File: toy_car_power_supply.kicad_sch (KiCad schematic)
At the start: 17 parts, among them J1 Barrel_Jack_Switch, J2 Screw_Terminal_01x02, J3 Screw_Terminal_01x02, J4 Conn_01x03_Pin, J5 Conn_01x02_Pin, J6 Conn_01x03_Pin, J7 Conn_01x02_Pin, SW1 SW_Wuerth_450301014042, U1 LM317_TO-220, U2 LM7805_TO220

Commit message: Changes sheet name
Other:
- title: Kicad Power supply Board -> Power supply Board
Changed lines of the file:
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@@
   (paper "A4")
   (title_block
-    (title "Kicad Power supply Board")
+    (title "Power supply Board")
     (date "2024-07-30")
     (rev "1")

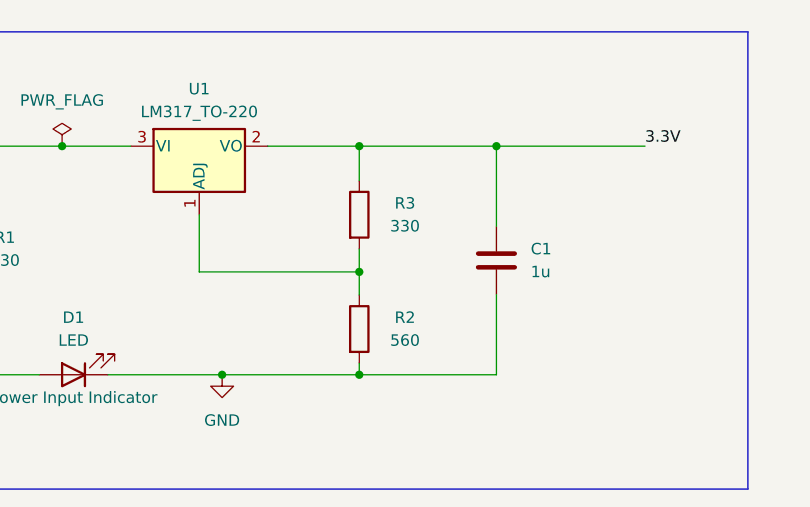
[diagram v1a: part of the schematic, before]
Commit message: Updated resistance value r1 = 270 r2 = 470
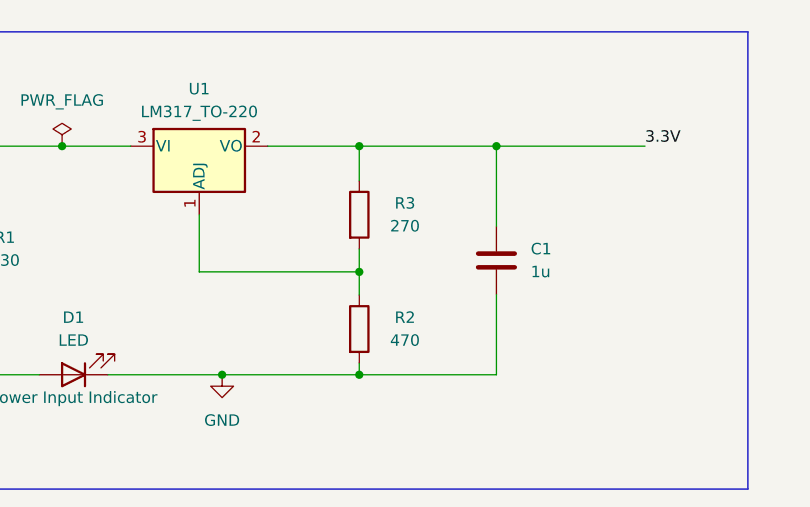
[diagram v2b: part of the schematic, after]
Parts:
- R2: value 560 -> 470
- R3: value 330 -> 270
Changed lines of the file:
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@@
       (effects (font (size 1.27 1.27)))
     )
-    (property "Value" "330" (at 91.44 114.3 0)
+    (property "Value" "270" (at 91.44 114.3 0)
       (effects (font (size 1.27 1.27)))
     )
@@
     (property "Datasheet" "~" (at 86.36 113.03 0)
       (effects (font (size 1.27 1.27)) hide)
+    )
+    (property "Purpose" "" (at 86.36 113.03 0)
+      (effects (font (size 1.27 1.27)))
     )
     (pin "1")
@@
       (effects (font (size 1.27 1.27)))
     )
-    (property "Value" "560" (at 91.44 127 0)
+    (property "Value" "470" (at 91.44 127 0)
       (effects (font (size 1.27 1.27)))
     )
@@
       (effects (font (size 1.27 1.27)) hide)
     )
+    (property "Purpose" "" (at 86.36 125.73 0)
+      (effects (font (size 1.27 1.27)))
+    )
     (pin "1")

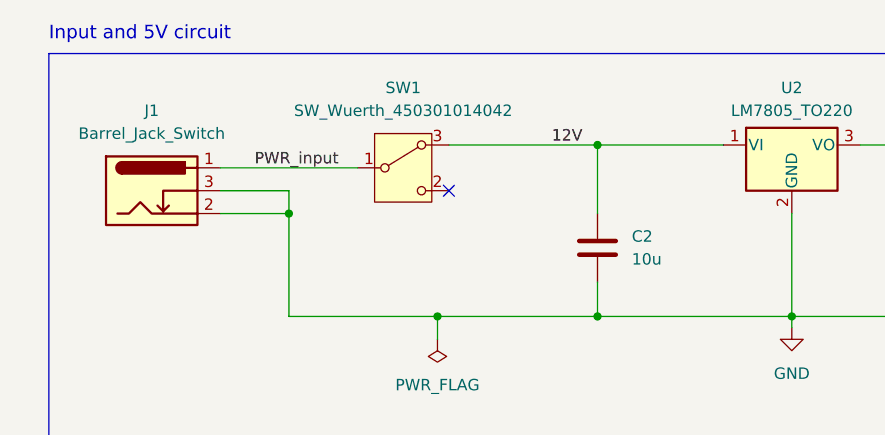
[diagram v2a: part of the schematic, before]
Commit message: Updated with custom switch with 4 pin
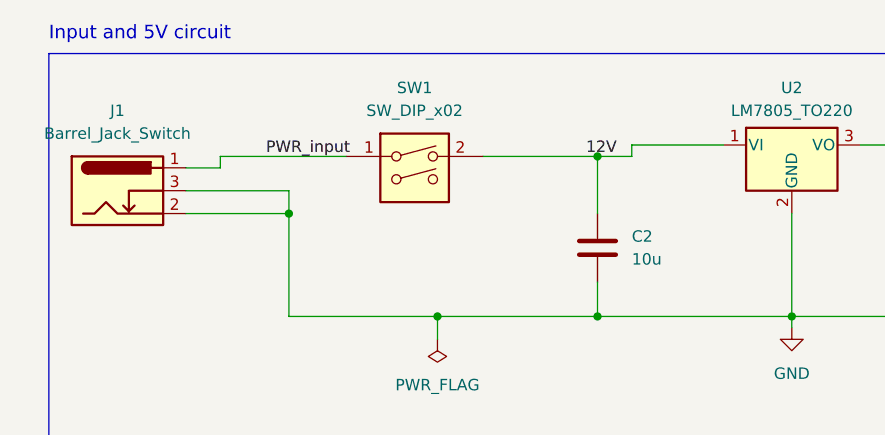
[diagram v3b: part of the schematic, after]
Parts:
- removed SW1: SW_Wuerth_450301014042, Button_Switch_THT:SW_Slide-03_Wuerth-WS-SLTV_10x2.5x6.4_P2.54mm, symbol Switch:SW_Wuerth_450301014042
- added SW1: SW_DIP_x02, custom_switch:DIP-4_W7.62mm, symbol custom_switch:SW_DIP_x02
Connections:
- net 12V: now also SW1.2
- net PWR_input: now also SW1.1
- no-connect marks 1 -> 0
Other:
- moved on the sheet: J1
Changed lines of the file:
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@@
     (company "Hobbyst")
   )
-  (junction (at 83.82 35.56) (diameter 0) (color 0 0 0 0)
-  )
   (junction (at 53.34 105.41) (diameter 0) (color 0 0 0 0)
   )
@@
   (junction (at 203.2 119.38) (diameter 0) (color 0 0 0 0)
   )
-  (no_connect (at 67.31 40.64))
+  (junction (at 83.82 36.83) (diameter 0) (color 0 0 0 0)
+  )
   (wire (pts (xy 223.52 90.17) (xy 214.63 90.17))
     (stroke (width 0) (type default))
   )
+  (wire (pts (xy 38.1 38.1) (xy 41.91 38.1))
+    (stroke (width 0) (type default))
+  )
   (wire (pts (xy 214.63 90.17) (xy 214.63 102.87))
     (stroke (width 0) (type default))
@@
     (stroke (width 0) (type default))
   )
+  (wire (pts (xy 41.91 36.83) (xy 55.88 36.83))
+    (stroke (width 0) (type default))
+  )
   (wire (pts (xy 41.91 120.65) (xy 41.91 130.81))
     (stroke (width 0) (type default))
@@
     (stroke (width 0) (type default))
   )
+  (wire (pts (xy 87.63 35.56) (xy 97.79 35.56))
+    (stroke (width 0) (type default))
+  )
   (wire (pts (xy 101.6 121.92) (xy 101.6 130.81))
     (stroke (width 0) (type default))
   )
-  (wire (pts (xy 41.91 40.64) (xy 49.53 40.64))
+  (wire (pts (xy 38.1 40.64) (xy 49.53 40.64))
     (stroke (width 0) (type default))
   )
@@
     (stroke (width 0) (type default))
   )
-  (wire (pts (xy 41.91 38.1) (xy 57.15 38.1))
-    (stroke (width 0) (type default))
-  )
   (wire (pts (xy 49.53 43.18) (xy 49.53 54.61))
     (stroke (width 0) (type default))
@@
     (stroke (width 0) (type default))
   )
+  (wire (pts (xy 83.82 36.83) (xy 87.63 36.83))
+    (stroke (width 0) (type default))
+  )
   (wire (pts (xy 203.2 57.15) (xy 203.2 71.12))
     (stroke (width 0) (type default))
@@
     (stroke (width 0) (type default))
   )
-  (wire (pts (xy 67.31 35.56) (xy 83.82 35.56))
+  (wire (pts (xy 71.12 36.83) (xy 83.82 36.83))
     (stroke (width 0) (type default))
   )
@@
     (stroke (width 0) (type default))
   )
-  (wire (pts (xy 41.91 43.18) (xy 49.53 43.18))
+  (wire (pts (xy 38.1 43.18) (xy 49.53 43.18))
     (stroke (width 0) (type default))
   )
@@
     (stroke (width 0) (type default))
   )
+  (wire (pts (xy 87.63 36.83) (xy 87.63 35.56))
+    (stroke (width 0) (type default))
+  )
   (polyline (pts (xy 177.8 142.24) (xy 259.08 142.24))
     (stroke (width 0) (type default))
@@
     (stroke (width 0) (type default))
   )
-  (wire (pts (xy 83.82 35.56) (xy 97.79 35.56))
-    (stroke (width 0) (type default))
-  )
   (wire (pts (xy 223.52 41.91) (xy 217.17 41.91))
     (stroke (width 0) (type default))
@@
     (stroke (width 0) (type default))
   )
+  (wire (pts (xy 41.91 36.83) (xy 41.91 38.1))
+    (stroke (width 0) (type default))
+  )
   (wire (pts (xy 134.62 35.56) (xy 148.59 35.56))
     (stroke (width 0) (type default))
   )
-  (wire (pts (xy 83.82 35.56) (xy 83.82 43.18))
+  (wire (pts (xy 83.82 36.83) (xy 83.82 43.18))
     (stroke (width 0) (type default))
   )
@@
     (effects (font (size 1.27 1.27)) (justify left bottom))
   )
-  (label "12V" (at 78.74 35.56 0) (fields_autoplaced)
+  (label "12V" (at 82.55 36.83 0) (fields_autoplaced)
     (effects (font (size 1.27 1.27)) (justify left bottom))
   )
-  (label "PWR_input" (at 45.72 38.1 0) (fields_autoplaced)
+  (label "PWR_input" (at 46.99 36.83 0) (fields_autoplaced)
     (effects (font (size 1.27 1.27)) (justify left bottom))
   )
@@
     )
   )
-  (symbol (lib_id "Connector:Barrel_Jack_Switch") (at 34.29 40.64 0) (unit 1)
-    (in_bom yes) (on_board yes) (dnp no) (fields_autoplaced)
-    (property "Reference" "J1" (at 34.29 31.75 0)
-      (effects (font (size 1.27 1.27)))
-    )
-    (property "Value" "Barrel_Jack_Switch" (at 34.29 34.29 0)
-      (effects (font (size 1.27 1.27)))
-    )
-    (property "Footprint" "Connector_BarrelJack:BarrelJack_Horizontal" (at 35.56 41.656 0)
-      (effects (font (size 1.27 1.27)) hide)
-    )
-    (property "Datasheet" "~" (at 35.56 41.656 0)
+  (symbol (lib_id "Connector:Barrel_Jack_Switch") (at 30.48 40.64 0) (unit 1)
+    (in_bom yes) (on_board yes) (dnp no) (fields_autoplaced)
+    (property "Reference" "J1" (at 30.48 31.75 0)
+      (effects (font (size 1.27 1.27)))
+    )
+    (property "Value" "Barrel_Jack_Switch" (at 30.48 34.29 0)
+      (effects (font (size 1.27 1.27)))
+    )
+    (property "Footprint" "Connector_BarrelJack:BarrelJack_Horizontal" (at 31.75 41.656 0)
+      (effects (font (size 1.27 1.27)) hide)
+    )
+    (property "Datasheet" "~" (at 31.75 41.656 0)
       (effects (font (size 1.27 1.27)) hide)
     )
@@
         (path "/851bce0c-ad2e-40a1-8b63-d2e380db4fe0"
           (reference "J6") (unit 1)
+        )
+      )
+    )
+  )
+  (symbol (lib_id "custom_switch:SW_DIP_x02") (at 63.5 39.37 0) (unit 1)
+    (in_bom yes) (on_board yes) (dnp no) (fields_autoplaced)
+    (property "Reference" "SW1" (at 63.5 29.21 0)
+      (effects (font (size 1.27 1.27)))
+    )
+    (property "Value" "SW_DIP_x02" (at 63.5 31.75 0)
+      (effects (font (size 1.27 1.27)))
+    )
+    (property "Footprint" "custom_switch:DIP-4_W7.62mm" (at 63.5 39.37 0)
+      (effects (font (size 1.27 1.27)) hide)
+    )
+    (property "Datasheet" "~" (at 63.5 39.37 0)
+      (effects (font (size 1.27 1.27)) hide)
+    )
+    (pin "1")
+    (pin "2")
+    (instances
+      (project "toy_car_power_supply"
+        (path "/851bce0c-ad2e-40a1-8b63-d2e380db4fe0"
+          (reference "SW1") (unit 1)
         )
       )
@@
         )
       )
-    )
-  )
-  (symbol (lib_id "Switch:SW_Wuerth_450301014042") (at 62.23 38.1 0) (unit 1)
-    (in_bom yes) (on_board yes) (dnp no) (fields_autoplaced)
-    (property "Reference" "SW1" (at 62.23 29.21 0)
-      (effects (font (size 1.27 1.27)))
-    )
-    (property "Value" "SW_Wuerth_450301014042" (at 62.23 31.75 0)
-      (effects (font (size 1.27 1.27)))
-    )
-    (property "Footprint" "Button_Switch_THT:SW_Slide-03_Wuerth-WS-SLTV_10x2.5x6.4_P2.54mm" (at 62.23 48.26 0)
-      (effects (font (size 1.27 1.27)) hide)
-    )
-    (property "Datasheet" "https://www.we-online.com/components/products/datasheet/450301014042.pdf" (at 62.23 45.72 0)
-      (effects (font (size 1.27 1.27)) hide)
-    )
-    (pin "1")
-    (pin "3")
-    (pin "2")
-    (instances
-      (project "toy_car_power_supply"
-        (path "/851bce0c-ad2e-40a1-8b63-d2e380db4fe0"
-          (reference "SW1") (unit 1)
-        )
-      )

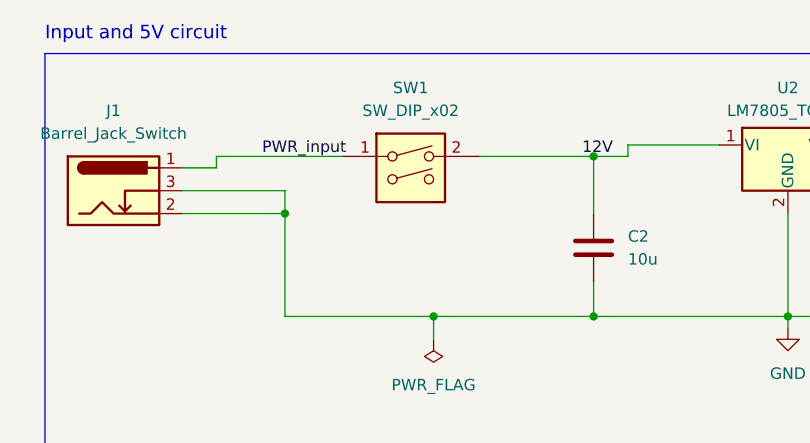
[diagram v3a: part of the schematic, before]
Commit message: Remove redundant library
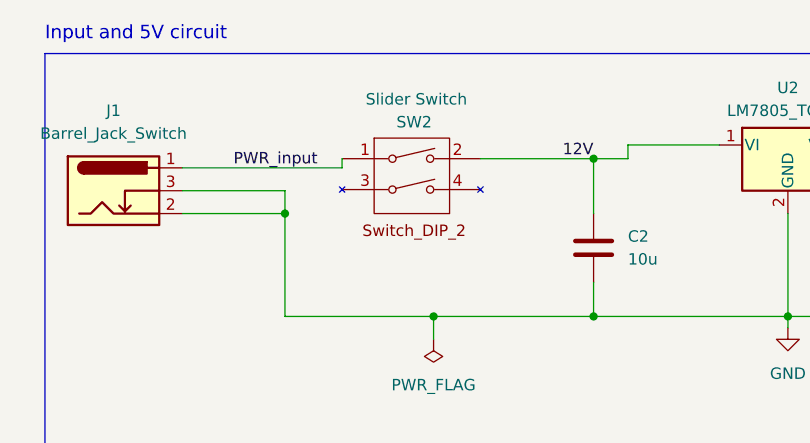
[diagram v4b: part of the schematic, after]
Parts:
- removed SW1: SW_DIP_x02, custom_switch:DIP-4_W7.62mm, symbol custom_switch:SW_DIP_x02
- added SW2: Slider Switch, custom_switch:DIP-4_W7.62mm, symbol custom_2DIP_switch:switch_2_DIP
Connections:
- net 12V: now also SW2.2
- net PWR_input: now also SW2.1
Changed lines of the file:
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@@
     (company "Hobbyst")
   )
+  (junction (at 83.82 37.084) (diameter 0) (color 0 0 0 0)
+  )
   (junction (at 53.34 105.41) (diameter 0) (color 0 0 0 0)
   )
@@
   (junction (at 203.2 119.38) (diameter 0) (color 0 0 0 0)
   )
-  (junction (at 83.82 36.83) (diameter 0) (color 0 0 0 0)
+  (wire (pts (xy 55.88 38.1) (xy 55.88 37.084))
+    (stroke (width 0) (type default))
   )
   (wire (pts (xy 223.52 90.17) (xy 214.63 90.17))
     (stroke (width 0) (type default))
   )
-  (wire (pts (xy 38.1 38.1) (xy 41.91 38.1))
+  (wire (pts (xy 38.1 38.1) (xy 55.88 38.1))
     (stroke (width 0) (type default))
   )
@@
     (stroke (width 0) (type default))
   )
-  (wire (pts (xy 41.91 36.83) (xy 55.88 36.83))
-    (stroke (width 0) (type default))
-  )
   (wire (pts (xy 41.91 120.65) (xy 41.91 130.81))
     (stroke (width 0) (type default))
@@
     (stroke (width 0) (type default))
   )
+  (wire (pts (xy 87.63 35.56) (xy 87.63 37.084))
+    (stroke (width 0) (type default))
+  )
   (polyline (pts (xy 129.54 143.51) (xy 25.4 143.51))
     (stroke (width 0) (type default))
@@
     (stroke (width 0) (type default))
   )
-  (wire (pts (xy 83.82 36.83) (xy 87.63 36.83))
-    (stroke (width 0) (type default))
-  )
   (wire (pts (xy 203.2 57.15) (xy 203.2 71.12))
     (stroke (width 0) (type default))
@@
     (stroke (width 0) (type default))
   )
-  (wire (pts (xy 71.12 36.83) (xy 83.82 36.83))
-    (stroke (width 0) (type default))
-  )
   (wire (pts (xy 134.62 35.56) (xy 134.62 43.18))
     (stroke (width 0) (type default))
@@
     (stroke (width 0) (type default))
   )
-  (wire (pts (xy 87.63 36.83) (xy 87.63 35.56))
-    (stroke (width 0) (type default))
-  )
   (polyline (pts (xy 177.8 142.24) (xy 259.08 142.24))
     (stroke (width 0) (type default))
   )
+  (wire (pts (xy 87.63 37.084) (xy 83.82 37.084))
+    (stroke (width 0) (type default))
+  )
   (wire (pts (xy 49.53 40.64) (xy 49.53 43.18))
     (stroke (width 0) (type default))
@@
     (stroke (width 0) (type default))
   )
+  (wire (pts (xy 71.247 37.084) (xy 83.82 37.084))
+    (stroke (width 0) (type default))
+  )
   (wire (pts (xy 68.58 119.38) (xy 86.36 119.38))
     (stroke (width 0) (type default))
@@
     (stroke (width 0) (type default))
   )
-  (wire (pts (xy 41.91 36.83) (xy 41.91 38.1))
+  (wire (pts (xy 83.82 37.084) (xy 83.82 43.18))
     (stroke (width 0) (type default))
   )
   (wire (pts (xy 134.62 35.56) (xy 148.59 35.56))
-    (stroke (width 0) (type default))
-  )
-  (wire (pts (xy 83.82 36.83) (xy 83.82 43.18))
     (stroke (width 0) (type default))
   )
@@
     (effects (font (size 1.27 1.27)) (justify left bottom))
   )
-  (label "12V" (at 82.55 36.83 0) (fields_autoplaced)
+  (label "12V" (at 80.391 37.084 0) (fields_autoplaced)
     (effects (font (size 1.27 1.27)) (justify left bottom))
   )
-  (label "PWR_input" (at 46.99 36.83 0) (fields_autoplaced)
+  (label "PWR_input" (at 43.815 38.1 0) (fields_autoplaced)
     (effects (font (size 1.27 1.27)) (justify left bottom))
   )
@@
     )
   )
-  (symbol (lib_id "custom_switch:SW_DIP_x02") (at 63.5 39.37 0) (unit 1)
-    (in_bom yes) (on_board yes) (dnp no) (fields_autoplaced)
-    (property "Reference" "SW1" (at 63.5 29.21 0)
-      (effects (font (size 1.27 1.27)))
-    )
-    (property "Value" "SW_DIP_x02" (at 63.5 31.75 0)
-      (effects (font (size 1.27 1.27)))
-    )
-    (property "Footprint" "custom_switch:DIP-4_W7.62mm" (at 63.5 39.37 0)
-      (effects (font (size 1.27 1.27)) hide)
-    )
-    (property "Datasheet" "~" (at 63.5 39.37 0)
-      (effects (font (size 1.27 1.27)) hide)
-    )
-    (pin "1")
-    (pin "2")
-    (instances
-      (project "toy_car_power_supply"
-        (path "/851bce0c-ad2e-40a1-8b63-d2e380db4fe0"
-          (reference "SW1") (unit 1)
-        )
-      )
+  (symbol (lib_id "custom_2DIP_switch:switch_2_DIP") (at 54.61 36.83 0) (unit 1)
+    (in_bom yes) (on_board yes) (dnp no)
+    (property "Reference" "SW2" (at 63.881 33.02 0)
+      (effects (font (size 1.27 1.27)))
+    )
+    (property "Value" "Slider Switch " (at 64.135 30.48 0)
+      (effects (font (size 1.27 1.27)))
+    )
+    (property "Footprint" "custom_switch:DIP-4_W7.62mm" (at 63.5 39.116 0)
+      (effects (font (size 1.27 1.27)) hide)
+    )
+    (property "Datasheet" "" (at 63.5 39.116 0)
+      (effects (font (size 1.27 1.27)) hide)
+    )
+    (property "Purpose" "" (at 54.61 36.83 0)
+      (effects (font (size 1.27 1.27)))
+    )
+    (pin "2")
+    (pin "3")
+    (pin "1")
+    (pin "4")
+    (instances
+      (project "toy_car_power_supply"
+        (path "/851bce0c-ad2e-40a1-8b63-d2e380db4fe0"
+          (reference "SW2") (unit 1)
+        )
+      )

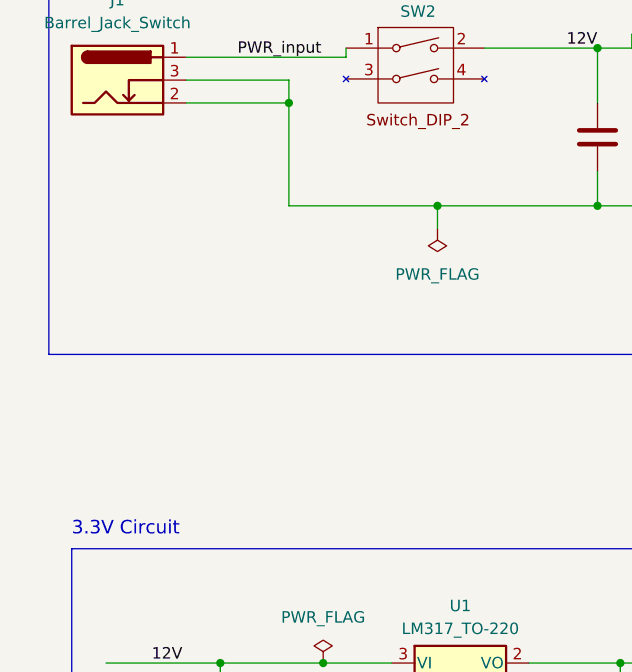
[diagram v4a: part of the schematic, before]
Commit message: Added conector for 12 v supply
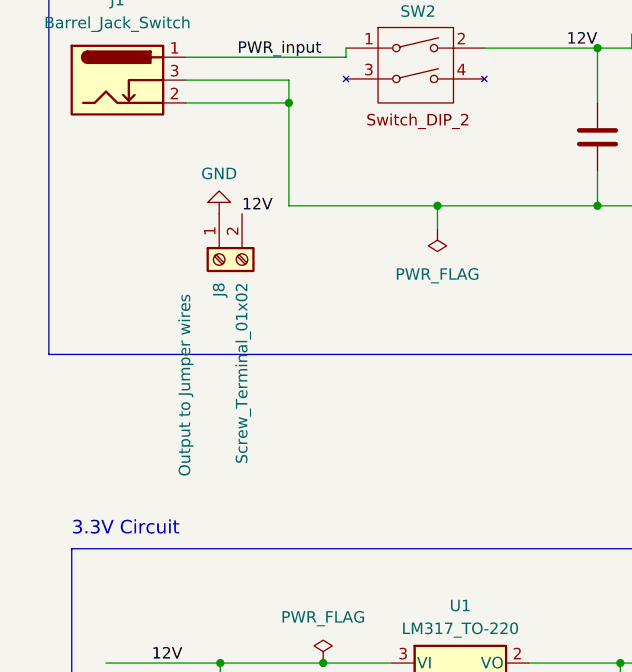
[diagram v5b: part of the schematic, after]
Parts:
- added J8: Screw_Terminal_01x02, TerminalBlock:TerminalBlock_bornier-2_P5.08mm, symbol Connector:Screw_Terminal_01x02
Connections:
- net 12V: now also J8.2 (Pin_2)
- net GND: now also J8.1 (Pin_1)
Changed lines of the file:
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@@
+    (effects (font (size 1.27 1.27)) (justify left bottom))
+  )
+  (label "12V" (at 44.323 55.499 0) (fields_autoplaced)
     (effects (font (size 1.27 1.27)) (justify left bottom))
   )
@@
         )
       )
+    )
+  )
+  (symbol (lib_id "power:GND") (at 41.783 55.499 180) (unit 1)
+    (in_bom yes) (on_board yes) (dnp no) (fields_autoplaced)
+    (property "Reference" "#PWR05" (at 41.783 49.149 0)
+      (effects (font (size 1.27 1.27)) hide)
+    )
+    (property "Value" "GND" (at 41.783 51.054 0)
+      (effects (font (size 1.27 1.27)))
+    )
+    (property "Footprint" "" (at 41.783 55.499 0)
+      (effects (font (size 1.27 1.27)) hide)
+    )
+    (property "Datasheet" "" (at 41.783 55.499 0)
+      (effects (font (size 1.27 1.27)) hide)
+    )
+    (pin "1")
+    (instances
+      (project "toy_car_power_supply"
+        (path "/851bce0c-ad2e-40a1-8b63-d2e380db4fe0"
+          (reference "#PWR05") (unit 1)
+        )
+      )
+    )
+  )
+  (symbol (lib_id "Connector:Screw_Terminal_01x02") (at 41.783 60.579 90) (mirror x) (unit 1)
+    (in_bom yes) (on_board yes) (dnp no)
+    (property "Reference" "J8" (at 41.783 63.119 0)
+      (effects (font (size 1.27 1.27)) (justify left))
+    )
+    (property "Value" "Screw_Terminal_01x02" (at 44.323 63.119 0)
+      (effects (font (size 1.27 1.27)) (justify left))
+    )
+    (property "Footprint" "TerminalBlock:TerminalBlock_bornier-2_P5.08mm" (at 41.783 60.579 0)
+      (effects (font (size 1.27 1.27)) hide)
+    )
+    (property "Datasheet" "~" (at 41.783 60.579 0)
+      (effects (font (size 1.27 1.27)) hide)
+    )
+    (property "Purpose" "Output to Jumper wires" (at 37.973 74.549 0)
+      (effects (font (size 1.27 1.27)))
+    )
+    (pin "1")
+    (pin "2")
+    (instances
+      (project "toy_car_power_supply"
+        (path "/851bce0c-ad2e-40a1-8b63-d2e380db4fe0"
+          (reference "J8") (unit 1)
+        )
+      )
